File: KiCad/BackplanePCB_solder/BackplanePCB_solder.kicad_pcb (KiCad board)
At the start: 2 copper layers, 470 x 55 mm, 54 parts, among them J1 PowerBug_GND, J10 Conn_02x05_Odd_Even, J11 DB15_Female_MountingHoles, J12 DB15_Female_MountingHoles, J13 DB15_Female_MountingHoles, J14 DB15_Female_MountingHoles, J15 DB15_Female_MountingHoles, J16 Conn_01x03, J17 Conn_01x03, J18 Conn_01x03, J19 Conn_01x03, J2 Conn_01x03, J20 Conn_01x03, J21 Conn_01x03, J22 Conn_01x03, J23 Conn_01x03, J24 Conn_01x03, J25 Conn_01x03, J3 PowerBug+17V, J4 Conn_02x05_Odd_Even, J5 DB15_Female_MountingHoles, J6 DB15_Female_MountingHoles, J7 DB15_Female_MountingHoles, J8 DB15_Female_MountingHoles, J9 DB15_Female_MountingHoles

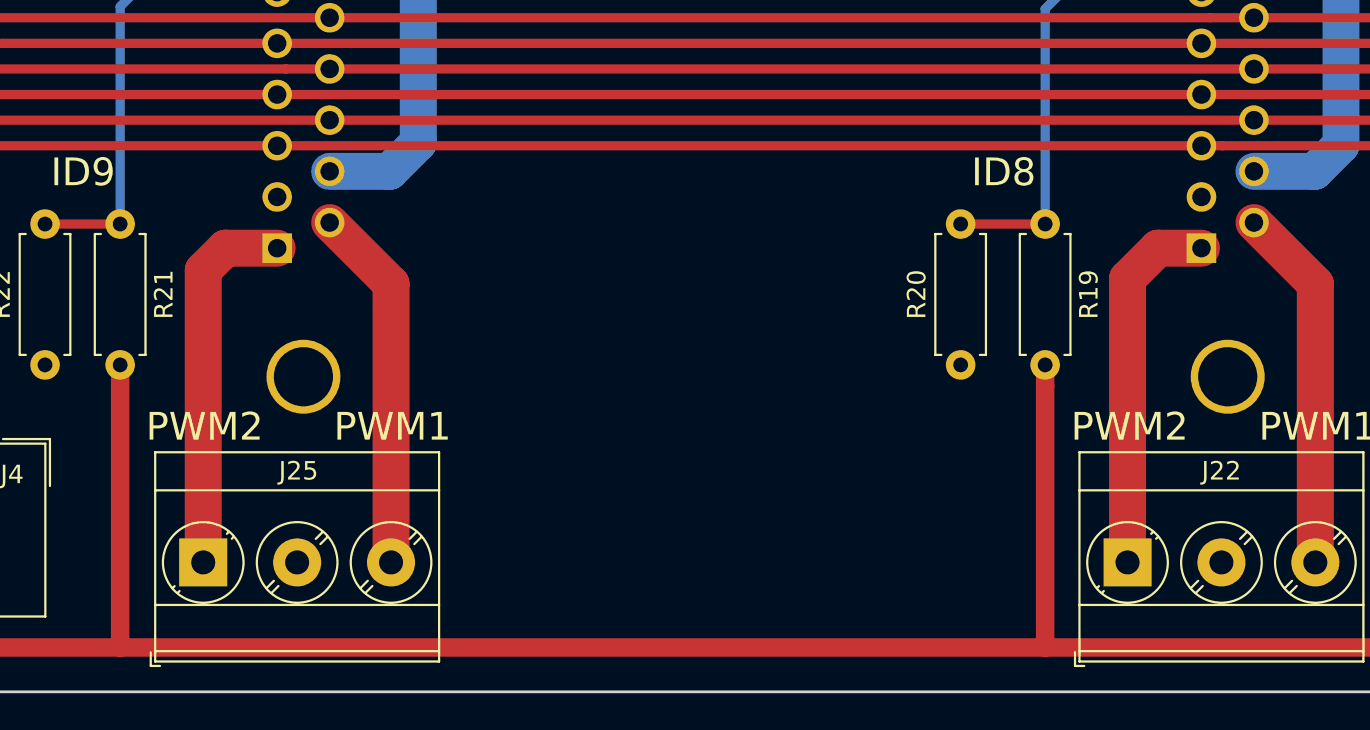
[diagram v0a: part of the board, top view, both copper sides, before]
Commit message: updated with bias resistors.
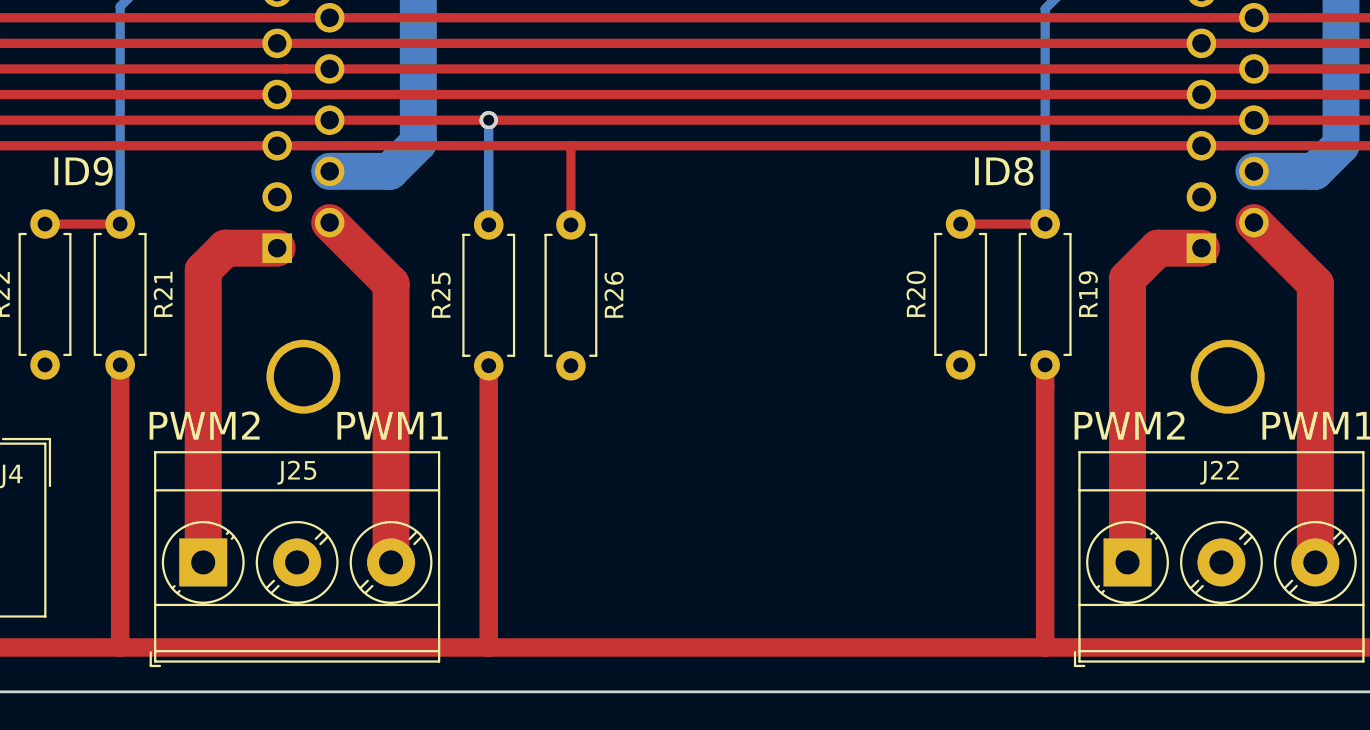
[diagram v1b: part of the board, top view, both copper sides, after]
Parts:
- added R25: 4k, Resistor_THT:R_Axial_DIN0207_L6.3mm_D2.5mm_P7.62mm_Horizontal, F.Cu at (131.4, 205.7)
- added R26: 1k, Resistor_THT:R_Axial_DIN0207_L6.3mm_D2.5mm_P7.62mm_Horizontal, F.Cu at (135.9, 205.7)
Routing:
- net +5V: track 608.4 -> 623.6 mm
- net /RX_A: track 512.6 -> 518.3 mm, vias 2 -> 3
- net /RX_B: track 520.6 -> 524.8 mm
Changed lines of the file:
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@@
-(kicad_pcb (version 20171130) (host pcbnew "(5.0.0-rc2-dev-444-g2974a2c10)")
+(kicad_pcb (version 20171130) (host pcbnew "(5.0.0-rc2-dev-451-g0294e41cb)")
   (general
     (thickness 1.6)
     (drawings 67)
-    (tracks 434)
+    (tracks 442)
     (zones 0)
-    (modules 54)
+    (modules 56)
     (nets 53)
   )
@@
   )
   (setup
-    (last_trace_width 0.25)
+    (last_trace_width 0.5)
     (user_trace_width 0.1)
     (user_trace_width 0.25)
@@
     )
   )
+  (module Resistor_THT:R_Axial_DIN0207_L6.3mm_D2.5mm_P7.62mm_Horizontal (layer F.Cu)
+    (at 131.445 205.74 270)
+    (descr "Resistor, Axial_DIN0207 series, Axial, Horizontal, pin pitch=7.62mm, 0.25W = 1/4W, length*diameter=6.3*2.5mm^2, http://cdn-reichelt.de/documents/datenblatt/B400/1_4W%23YAG.pdf")
+    (tags "Resistor Axial_DIN0207 series Axial Horizontal pin pitch 7.62mm 0.25W = 1/4W length 6.3mm diameter 2.5mm")
+    (fp_text reference R25 (at 3.81 2.54 270) (layer F.SilkS)
+      (effects (font (size 1 1) (thickness 0.15)))
+    )
+    (fp_text value 4k (at 3.81 2.37 270) (layer F.Fab)
+      (effects (font (size 1 1) (thickness 0.15)))
+    )
+    (fp_line (start 0.66 -1.25) (end 0.66 1.25) (layer F.Fab) (width 0.1))
+    (fp_line (start 0.66 1.25) (end 6.96 1.25) (layer F.Fab) (width 0.1))
+    (fp_line (start 6.96 1.25) (end 6.96 -1.25) (layer F.Fab) (width 0.1))
+    (fp_line (start 6.96 -1.25) (end 0.66 -1.25) (layer F.Fab) (width 0.1))
+    (fp_line (start 0 0) (end 0.66 0) (layer F.Fab) (width 0.1))
+    (fp_line (start 7.62 0) (end 6.96 0) (layer F.Fab) (width 0.1))
+    (fp_line (start 0.54 -1.04) (end 0.54 -1.37) (layer F.SilkS) (width 0.12))
+    (fp_line (start 0.54 -1.37) (end 7.08 -1.37) (layer F.SilkS) (width 0.12))
+    (fp_line (start 7.08 -1.37) (end 7.08 -1.04) (layer F.SilkS) (width 0.12))
+    (fp_line (start 0.54 1.04) (end 0.54 1.37) (layer F.SilkS) (width 0.12))
+    (fp_line (start 0.54 1.37) (end 7.08 1.37) (layer F.SilkS) (width 0.12))
+    (fp_line (start 7.08 1.37) (end 7.08 1.04) (layer F.SilkS) (width 0.12))
+    (fp_line (start -1.05 -1.65) (end -1.05 1.65) (layer F.CrtYd) (width 0.05))
+    (fp_line (start -1.05 1.65) (end 8.7 1.65) (layer F.CrtYd) (width 0.05))
+    (fp_line (start 8.7 1.65) (end 8.7 -1.65) (layer F.CrtYd) (width 0.05))
+    (fp_line (start 8.7 -1.65) (end -1.05 -1.65) (layer F.CrtYd) (width 0.05))
+    (fp_text user %R (at 3.81 0 270) (layer F.Fab)
+      (effects (font (size 1 1) (thickness 0.15)))
+    )
+    (pad 1 thru_hole circle (at 0 0 270) (size 1.6 1.6) (drill 0.8) (layers *.Cu *.Mask)
+      (net 7 /RX_A))
+    (pad 2 thru_hole oval (at 7.62 0 270) (size 1.6 1.6) (drill 0.8) (layers *.Cu *.Mask)
+      (net 13 +5V))
+    (model ${KISYS3DMOD}/Resistor_THT.3dshapes/R_Axial_DIN0207_L6.3mm_D2.5mm_P7.62mm_Horizontal.wrl
+      (at (xyz 0 0 0))
+      (scale (xyz 1 1 1))
+      (rotate (xyz 0 0 0))
+    )
+  )
+  (module Resistor_THT:R_Axial_DIN0207_L6.3mm_D2.5mm_P7.62mm_Horizontal (layer F.Cu)
+    (at 135.89 205.74 270)
+    (descr "Resistor, Axial_DIN0207 series, Axial, Horizontal, pin pitch=7.62mm, 0.25W = 1/4W, length*diameter=6.3*2.5mm^2, http://cdn-reichelt.de/documents/datenblatt/B400/1_4W%23YAG.pdf")
+    (tags "Resistor Axial_DIN0207 series Axial Horizontal pin pitch 7.62mm 0.25W = 1/4W length 6.3mm diameter 2.5mm")
+    (fp_text reference R26 (at 3.81 -2.37 270) (layer F.SilkS)
+      (effects (font (size 1 1) (thickness 0.15)))
+    )
+    (fp_text value 1k (at 3.81 2.37 270) (layer F.Fab)
+      (effects (font (size 1 1) (thickness 0.15)))
+    )
+    (fp_text user %R (at 3.81 0 270) (layer F.Fab)
+      (effects (font (size 1 1) (thickness 0.15)))
+    )
+    (fp_line (start 8.7 -1.65) (end -1.05 -1.65) (layer F.CrtYd) (width 0.05))
+    (fp_line (start 8.7 1.65) (end 8.7 -1.65) (layer F.CrtYd) (width 0.05))
+    (fp_line (start -1.05 1.65) (end 8.7 1.65) (layer F.CrtYd) (width 0.05))
+    (fp_line (start -1.05 -1.65) (end -1.05 1.65) (layer F.CrtYd) (width 0.05))
+    (fp_line (start 7.08 1.37) (end 7.08 1.04) (layer F.SilkS) (width 0.12))
+    (fp_line (start 0.54 1.37) (end 7.08 1.37) (layer F.SilkS) (width 0.12))
+    (fp_line (start 0.54 1.04) (end 0.54 1.37) (layer F.SilkS) (width 0.12))
+    (fp_line (start 7.08 -1.37) (end 7.08 -1.04) (layer F.SilkS) (width 0.12))
+    (fp_line (start 0.54 -1.37) (end 7.08 -1.37) (layer F.SilkS) (width 0.12))
+    (fp_line (start 0.54 -1.04) (end 0.54 -1.37) (layer F.SilkS) (width 0.12))
+    (fp_line (start 7.62 0) (end 6.96 0) (layer F.Fab) (width 0.1))
+    (fp_line (start 0 0) (end 0.66 0) (layer F.Fab) (width 0.1))
+    (fp_line (start 6.96 -1.25) (end 0.66 -1.25) (layer F.Fab) (width 0.1))
+    (fp_line (start 6.96 1.25) (end 6.96 -1.25) (layer F.Fab) (width 0.1))
+    (fp_line (start 0.66 1.25) (end 6.96 1.25) (layer F.Fab) (width 0.1))
+    (fp_line (start 0.66 -1.25) (end 0.66 1.25) (layer F.Fab) (width 0.1))
+    (pad 2 thru_hole oval (at 7.62 0 270) (size 1.6 1.6) (drill 0.8) (layers *.Cu *.Mask)
+      (net 9 GND))
+    (pad 1 thru_hole circle (at 0 0 270) (size 1.6 1.6) (drill 0.8) (layers *.Cu *.Mask)
+      (net 8 /RX_B))
+    (model ${KISYS3DMOD}/Resistor_THT.3dshapes/R_Axial_DIN0207_L6.3mm_D2.5mm_P7.62mm_Horizontal.wrl
+      (at (xyz 0 0 0))
+      (scale (xyz 1 1 1))
+      (rotate (xyz 0 0 0))
+    )
+  )
   (gr_text "RS485 Termination" (at 66.3 197.2 90) (layer F.SilkS)
     (effects (font (size 1.5 1.5) (thickness 0.3)))
@@
   (segment (start 62.008 203.132) (end 64.584 203.132) (width 0.5) (layer F.Cu) (net 7))
   (segment (start 64.584 203.132) (end 67.641 200.075) (width 0.5) (layer F.Cu) (net 7))
-  (segment (start 122.84 200.075) (end 172.84 200.075) (width 0.5) (layer F.Cu) (net 7))
   (segment (start 222.84 200.075) (end 172.84 200.075) (width 0.5) (layer F.Cu) (net 7))
   (segment (start 222.84 200.075) (end 272.84 200.075) (width 0.5) (layer F.Cu) (net 7))
@@
   (segment (start 91.948 223.52) (end 90.678 223.52) (width 0.5) (layer B.Cu) (net 7))
   (segment (start 90.678 223.52) (end 89.662 222.504) (width 0.5) (layer B.Cu) (net 7))
-  (segment (start 120 201.46) (end 170 201.46) (width 0.5) (layer F.Cu) (net 8))
+  (segment (start 131.445 205.74) (end 131.445 200.025) (width 0.5) (layer B.Cu) (net 7))
+  (via (at 131.445 200.075) (size 1) (drill 0.6) (layers F.Cu B.Cu) (net 7))
+  (segment (start 131.445 200.025) (end 131.445 200.075) (width 0.5) (layer B.Cu) (net 7))
+  (segment (start 122.84 200.075) (end 131.445 200.075) (width 0.5) (layer F.Cu) (net 7))
+  (segment (start 131.445 200.075) (end 172.84 200.075) (width 0.5) (layer F.Cu) (net 7))
   (segment (start 171.13137 201.46) (end 220 201.46) (width 0.5) (layer F.Cu) (net 8))
   (segment (start 170 201.46) (end 171.13137 201.46) (width 0.5) (layer F.Cu) (net 8))
@@
   (segment (start 94.488 223.52) (end 92.456 225.552) (width 0.5) (layer B.Cu) (net 8))
   (segment (start 92.456 225.552) (end 90.424 225.552) (width 0.5) (layer B.Cu) (net 8))
+  (segment (start 135.89 205.74) (end 135.89 201.46) (width 0.5) (layer F.Cu) (net 8))
+  (segment (start 120 201.46) (end 135.89 201.46) (width 0.5) (layer F.Cu) (net 8))
+  (segment (start 135.89 201.46) (end 170 201.46) (width 0.5) (layer F.Cu) (net 8))
   (segment (start 72.84 202.845) (end 75.92 202.845) (width 2) (layer B.Cu) (net 10))
   (segment (start 75.92 202.845) (end 77.47 201.295) (width 2) (layer B.Cu) (net 10))
@@
   (segment (start 281.432 228.473) (end 281.305 228.6) (width 1) (layer F.Cu) (net 13))
   (segment (start 111.506 213.314) (end 111.506 228.6) (width 1) (layer F.Cu) (net 13))
-  (segment (start 111.506 228.6) (end 161.544 228.6) (width 1) (layer F.Cu) (net 13))
   (segment (start 211.328 214.44537) (end 211.328 228.6) (width 1) (layer F.Cu) (net 13))
   (segment (start 211.328 213.314) (end 211.328 214.44537) (width 1) (layer F.Cu) (net 13))
@@
   (segment (start 281.305 228.6) (end 261.112 228.6) (width 1) (layer F.Cu) (net 13))
   (segment (start 261.112 228.6) (end 211.328 228.6) (width 1) (layer F.Cu) (net 13))
+  (segment (start 131.445 213.36) (end 131.445 228.6) (width 1) (layer F.Cu) (net 13))
+  (segment (start 111.506 228.6) (end 131.445 228.6) (width 1) (layer F.Cu) (net 13))
+  (segment (start 131.445 228.6) (end 161.544 228.6) (width 1) (layer F.Cu) (net 13))
   (segment (start 517.2 207) (end 520 207) (width 2) (layer F.Cu) (net 14))
   (segment (start 516 208.2) (end 517.2 207) (width 2) (layer F.Cu) (net 14))
